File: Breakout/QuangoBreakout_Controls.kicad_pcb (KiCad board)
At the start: 2 copper layers, 18.8 x 110 mm, 37 parts, among them J1 Audio_Send_A, J10 Audio_Breakout, J2 Audio_Send_B, J3 Audio_Return_A, J4 Audio_Return_A, J6 Eurorack_10_pin_power, J7 JackMixA, J8 JackMixB, J9 JackMixBoth, U1 TL074

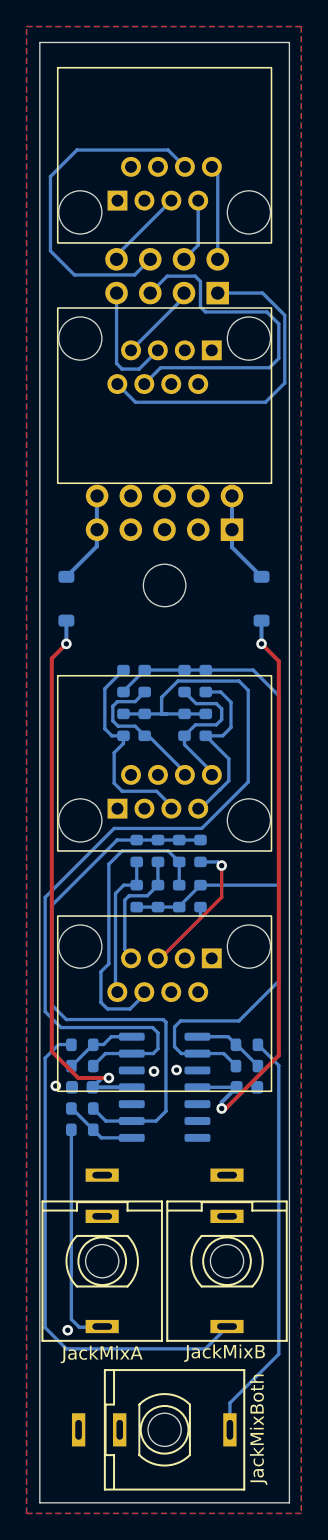
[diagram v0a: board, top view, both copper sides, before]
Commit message: Terminated unused op-amp
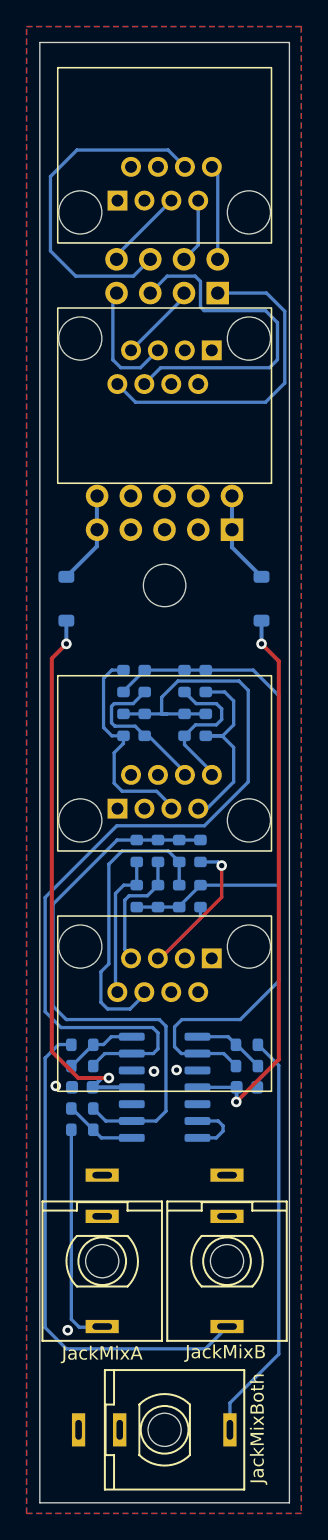
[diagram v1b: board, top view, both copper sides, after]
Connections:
- U1 pad 12: (no net) -> GND
- U1 pad 13: (no net) -> Net-(U1D--)
- U1 pad 14: (no net) -> Net-(U1D--)
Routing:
- net Net-(U1D--): track 0.00 -> 4.61 mm
- net -12V: track 44.3 -> 42.2 mm
- net /AudioB2_Return: track 13.4 -> 15.0 mm
- net /AudioB4_Return: track 15.8 -> 16.4 mm

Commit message: Added Breakout gerbers; Added pdfs of schematics
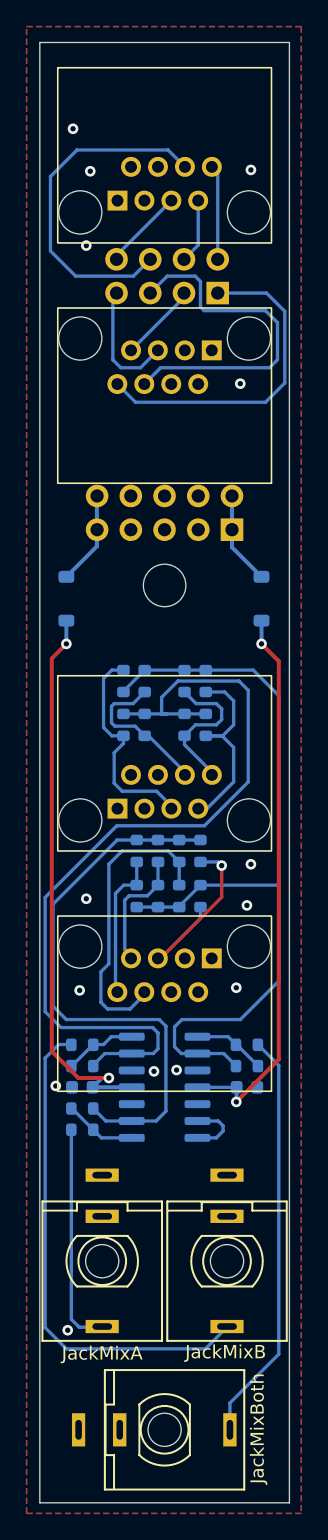
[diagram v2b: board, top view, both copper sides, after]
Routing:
- net GND: vias 4 -> 14
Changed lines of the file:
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@@
     (pad_to_mask_clearance 0)
     (pcbplotparams
-      (layerselection 0x00010fc_ffffffff)
+      (layerselection 0x00010f0_ffffffff)
       (plot_on_all_layers_selection 0x0000000_00000000)
       (disableapertmacros false)
@@
   (via (at 52.1 147) (size 0.8) (drill 0.4) (layers "F.Cu" "B.Cu") (free) (net 23))
   (via (at 60.3 127.4) (size 0.8) (drill 0.4) (layers "F.Cu" "B.Cu") (free) (net 23))
+  (via (at 65.9 111.9) (size 0.8) (drill 0.4) (layers "F.Cu" "B.Cu") (free) (net 23))
+  (via (at 65.6 115) (size 0.8) (drill 0.4) (layers "F.Cu" "B.Cu") (free) (net 23))
+  (via (at 53.5 65.3) (size 0.8) (drill 0.4) (layers "F.Cu" "B.Cu") (free) (net 23))
+  (via (at 53 121.4) (size 0.8) (drill 0.4) (layers "F.Cu" "B.Cu") (free) (net 23))
   (via (at 51.2 128.6) (size 0.8) (drill 0.4) (layers "F.Cu" "B.Cu") (free) (net 23))
+  (via (at 53.8 59.7) (size 0.8) (drill 0.4) (layers "F.Cu" "B.Cu") (free) (net 23))
+  (via (at 52.5 56.5) (size 0.8) (drill 0.4) (layers "F.Cu" "B.Cu") (free) (net 23))
+  (via (at 53.5 114.5) (size 0.8) (drill 0.4) (layers "F.Cu" "B.Cu") (free) (net 23))
+  (via (at 65.1 75.7) (size 0.8) (drill 0.4) (layers "F.Cu" "B.Cu") (free) (net 23))
+  (via (at 65.9 59.6) (size 0.8) (drill 0.4) (layers "F.Cu" "B.Cu") (free) (net 23))
   (via (at 58.6 127.5) (size 0.8) (drill 0.4) (layers "F.Cu" "B.Cu") (free) (net 23))
+  (via (at 64.8 121.2) (size 0.8) (drill 0.4) (layers "F.Cu" "B.Cu") (free) (net 23))
   (segment (start 55.2 119.4) (end 54.6 120) (width 0.25) (layer "B.Cu") (net 24))
   (segment (start 55.1 122.8) (end 56.8 122.8) (width 0.25) (layer "B.Cu") (net 24))
